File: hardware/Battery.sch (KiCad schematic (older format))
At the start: 14 parts, among them Q401 DMP2110UW-7, U401 LM66100, U402 MCP73831-2-OT, U403 TLV810E

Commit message: added order references to parts
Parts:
- R401, R402, R403: Manufacturer (none) -> TE Connectivity / Holsworthy; Order (none) -> https://www.mouser.at/ProductDetail/TE-Connectivity-Holswor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
- U403: Manufacturer (none) -> Texas Instruments; Order (none) -> https://www.mouser.at/ProductDetail/Texas-Instruments/TLV81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
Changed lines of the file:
@@
 F 2 "Resistor_SMD:R_0603_1608Metric" H 3250 2150 50  0001 C CNN
 F 3 "~" H 3250 2150 50  0001 C CNN
-F 4 "" H 3250 2150 50  0001 C CNN "Order"
+F 4 "https://www.mouser.at/ProductDetail/TE-Connectivity-Holsworthy/CRGP0603F3K9?qs=%2Fha2pyFaduj8qGn91HGzk%2F8kvmOrHSLEzveCoZJh19NXlgDLdxx7mg%3D%3D" H 3250 2150 50  0001 C CNN "Order"
+F 5 "TE Connectivity / Holsworthy" H 3250 2150 50  0001 C CNN "Manufacturer"
 	1    3250 2150
 	1    0    0    -1
@@
 F 2 "Package_TO_SOT_SMD:SOT-23" H 6150 2950 50  0001 C CNN
 F 3 "" H 6150 2950 50  0001 C CNN
+F 4 "Texas Instruments" H 5750 2250 50  0001 C CNN "Manufacturer"
+F 5 "https://www.mouser.at/ProductDetail/Texas-Instruments/TLV810EA29DBZR?qs=OlC7AqGiEDn%2F4%252BrWzJaHww%3D%3D" H 5750 2250 50  0001 C CNN "Order"
 	1    5750 2250
 	1    0    0    -1
@@
 F 2 "Resistor_SMD:R_0603_1608Metric" H 2650 2600 50  0001 C CNN
 F 3 "~" H 2650 2600 50  0001 C CNN
-F 4 "" H 2650 2600 50  0001 C CNN "Order"
+F 4 "https://www.mouser.at/ProductDetail/TE-Connectivity-Holsworthy/CRGP0603F2K7?qs=wUXugUrL1qwUN23XEDlhqg%3D%3D" H 2650 2600 50  0001 C CNN "Order"
+F 5 "TE Connectivity / Holsworthy" H 2650 2600 50  0001 C CNN "Manufacturer"
 	1    2650 2600
 	1    0    0    -1
@@
 F 2 "Resistor_SMD:R_0603_1608Metric" H 2650 3400 50  0001 C CNN
 F 3 "~" H 2650 3400 50  0001 C CNN
-F 4 "" H 2650 3400 50  0001 C CNN "Order"
+F 4 "https://www.mouser.at/ProductDetail/TE-Connectivity-Holsworthy/CRGP0603F2K7?qs=wUXugUrL1qwUN23XEDlhqg%3D%3D" H 2650 3400 50  0001 C CNN "Order"
+F 5 "TE Connectivity / Holsworthy" H 2650 3400 50  0001 C CNN "Manufacturer"
 	1    2650 3400
 	1    0    0    -1

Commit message: modified bom
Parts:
- BT401: value Battery_Cell -> LIPO
- C401, C402: MNR (none) -> CL10B106MQ8NRNC
- D401: MNR (none) -> AA1608SURSK
- D402: MNR (none) -> AA1608CGSK
- Q401: MNR (none) -> DMP2110UW-7
- R401, R402: MNR (none) -> CRGP0603F2K7
- R403: MNR (none) -> CRGP0603F3K9
- R404, R405: MNR (none) -> CRGP0603F47K
- U401: MNR (none) -> LM66100DCKR
- U402: MNR (none) -> MCP73831T-2ACI/OT
- U403: MNR (none) -> TLV810EA29DBZR
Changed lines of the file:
@@
 F 4 "https://www.mouser.at/ProductDetail/187-CL10B106MQ8NRNC" H 2950 1850 50  0001 C CNN "Order"
 F 5 "Samsung Electro-Mechanics" H 2950 1850 50  0001 C CNN "Manufacturer"
+F 6 "CL10B106MQ8NRNC" H 2950 1850 50  0001 C CNN "MNR"
 	1    2950 1850
 	1    0    0    -1
@@
 F 4 "https://www.mouser.at/ProductDetail/187-CL10B106MQ8NRNC" H 4400 1950 50  0001 C CNN "Order"
 F 5 "Samsung Electro-Mechanics" H 4400 1950 50  0001 C CNN "Manufacturer"
+F 6 "CL10B106MQ8NRNC" H 4400 1950 50  0001 C CNN "MNR"
 	1    4400 1950
 	1    0    0    -1
@@
 F 4 "https://www.mouser.at/ProductDetail/579-MCP73831T-2ACIOT" H 3750 1900 50  0001 C CNN "Order"
 F 5 "Microchip Technology" H 3750 1900 50  0001 C CNN "Manufacturer"
+F 6 "MCP73831T-2ACI/OT" H 3750 1900 50  0001 C CNN "MNR"
 	1    3750 1900
 	1    0    0    -1
@@
 F 4 "https://www.mouser.at/ProductDetail/TE-Connectivity-Holsworthy/CRGP0603F3K9?qs=%2Fha2pyFaduj8qGn91HGzk%2F8kvmOrHSLEzveCoZJh19NXlgDLdxx7mg%3D%3D" H 3250 2150 50  0001 C CNN "Order"
 F 5 "TE Connectivity / Holsworthy" H 3250 2150 50  0001 C CNN "Manufacturer"
+F 6 "CRGP0603F3K9" H 3250 2150 50  0001 C CNN "MNR"
 	1    3250 2150
 	1    0    0    -1
@@
 AR Path="/6063DAC2/60645BC2" Ref="BT401"  Part="1"
 F 0 "BT401" H 4868 2146 50  0000 L CNN
-F 1 "Battery_Cell" H 4868 2055 50  0000 L CNN
+F 1 "LIPO" H 4868 2055 50  0000 L CNN
 F 2 "Connector_PinHeader_2.54mm:PinHeader_1x02_P2.54mm_Vertical" V 4750 2110 50  0001 C CNN
 F 3 "~" V 4750 2110 50  0001 C CNN
@@
 F 4 "Diodes Incorporated" H 6200 1900 50  0001 C CNN "Manufacturer"
 F 5 "https://www.mouser.at/ProductDetail/Diodes-Incorporated/DMP2110UW-7?qs=bZr6mbWTK5lZsAURvLPe3w%3D%3D" H 6200 1900 50  0001 C CNN "Order"
+F 6 "DMP2110UW-7" H 6200 1900 50  0001 C CNN "MNR"
 	1    6200 1900
 	0    1    -1   0
@@
 F 4 "Texas Instruments" H 5750 2250 50  0001 C CNN "Manufacturer"
 F 5 "https://www.mouser.at/ProductDetail/Texas-Instruments/TLV810EA29DBZR?qs=OlC7AqGiEDn%2F4%252BrWzJaHww%3D%3D" H 5750 2250 50  0001 C CNN "Order"
+F 6 "TLV810EA29DBZR" H 5750 2250 50  0001 C CNN "MNR"
 	1    5750 2250
 	1    0    0    -1
@@
 F 4 "https://www.mouser.at/ProductDetail/279-CRGP0603F47K" H 6800 2300 50  0001 C CNN "Order"
 F 5 "TE Connectivity / Holsworthy" H 6800 2300 50  0001 C CNN "Manufacturer"
+F 6 "CRGP0603F47K" H 6800 2300 50  0001 C CNN "MNR"
 	1    6800 2300
 	1    0    0    -1
@@
 F 4 "https://www.mouser.at/ProductDetail/279-CRGP0603F47K" H 6800 2000 50  0001 C CNN "Order"
 F 5 "TE Connectivity / Holsworthy" H 6800 2000 50  0001 C CNN "Manufacturer"
+F 6 "CRGP0603F47K" H 6800 2000 50  0001 C CNN "MNR"
 	1    6800 2000
 	1    0    0    -1
@@
 F 4 "Texas Instruments" H 1950 1600 50  0001 C CNN "Manufacturer"
 F 5 "https://www.mouser.at/ProductDetail/595-LM66100DCKR" H 1950 1600 50  0001 C CNN "Order"
+F 6 "LM66100DCKR" H 1950 1600 50  0001 C CNN "MNR"
 	1    1950 1600
 	1    0    0    -1
@@
 F 5 "Kingbright" V 2650 2850 50  0001 C CNN "Manufacturer"
 F 6 "https://www.mouser.at/ProductDetail/Kingbright/AA1608SURSK?qs=eP2BKZSCXI6pqonvuMmTFg%3D%3D" H 2650 2850 50  0001 C CNN "Order"
+F 7 "AA1608SURSK" H 2650 2850 50  0001 C CNN "MNR"
 	1    2650 2850
 	0    -1   -1   0
@@
 F 4 "https://www.mouser.at/ProductDetail/TE-Connectivity-Holsworthy/CRGP0603F2K7?qs=wUXugUrL1qwUN23XEDlhqg%3D%3D" H 2650 2600 50  0001 C CNN "Order"
 F 5 "TE Connectivity / Holsworthy" H 2650 2600 50  0001 C CNN "Manufacturer"
+F 6 "CRGP0603F2K7" H 2650 2600 50  0001 C CNN "MNR"
 	1    2650 2600
 	1    0    0    -1
@@
 F 4 "https://www.mouser.at/ProductDetail/TE-Connectivity-Holsworthy/CRGP0603F2K7?qs=wUXugUrL1qwUN23XEDlhqg%3D%3D" H 2650 3400 50  0001 C CNN "Order"
 F 5 "TE Connectivity / Holsworthy" H 2650 3400 50  0001 C CNN "Manufacturer"
+F 6 "CRGP0603F2K7" H 2650 3400 50  0001 C CNN "MNR"
 	1    2650 3400
 	1    0    0    -1
@@
 F 5 "AA1608CGSK" H 2650 3150 50  0001 C CNN "Part Number"
 F 6 "https://www.mouser.at/ProductDetail/Kingbright/AA1608CGSK?qs=%2Fha2pyFadujroVvVMWEuOp8b2ZvB17TZCtvrJxnHY68n8r1EECXbcw%3D%3D" H 2650 3150 50  0001 C CNN "Order"
+F 7 "AA1608CGSK" H 2650 3150 50  0001 C CNN "MNR"
 	1    2650 3150
 	0    -1   -1   0

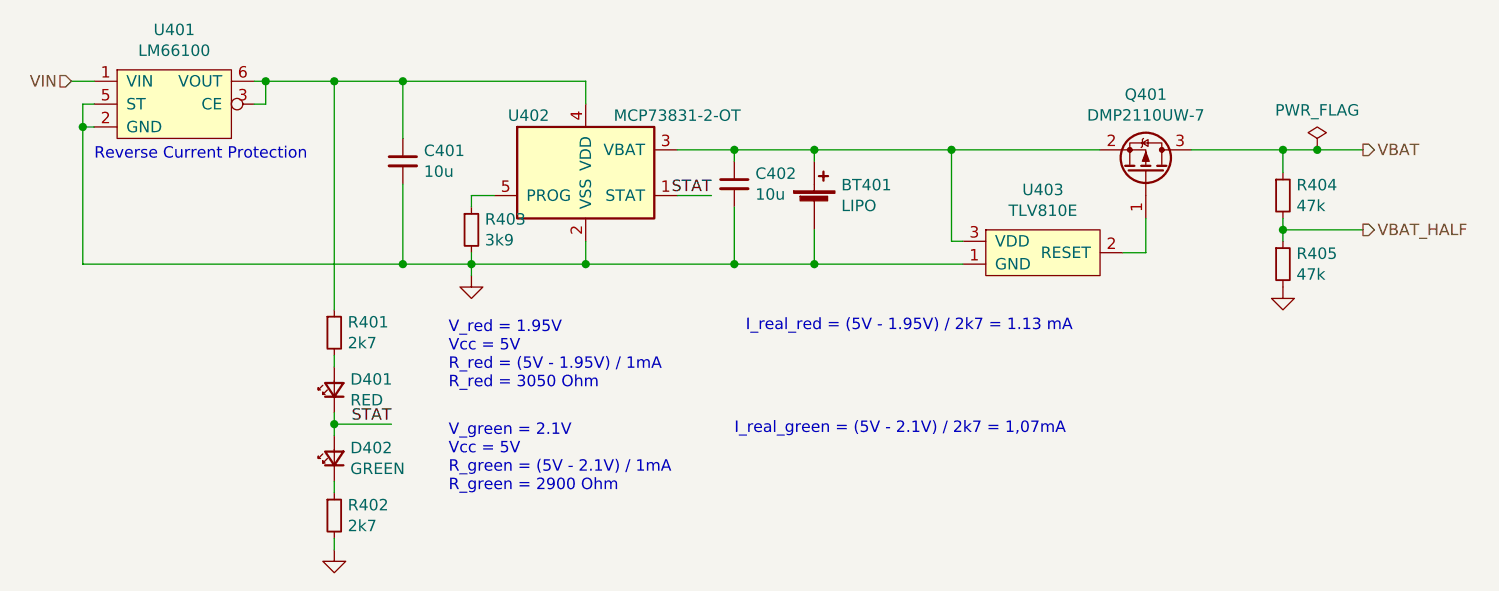
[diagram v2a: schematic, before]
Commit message: New uC, ditched FTDI chip, and more!
Need to improve the schematic a little bit more.
For example, I want to be able to turn the LED Drivers off using
a MOSFET.

For the PCB Layout: I want to move as many components as possible
to the top layer, so that they are visible when in the case.
Also, I have to consider solderability of the components, the more
complex should all be on one layer for easier soldering.

Next up: Finishing the schematic, improving component placement,
and routing!
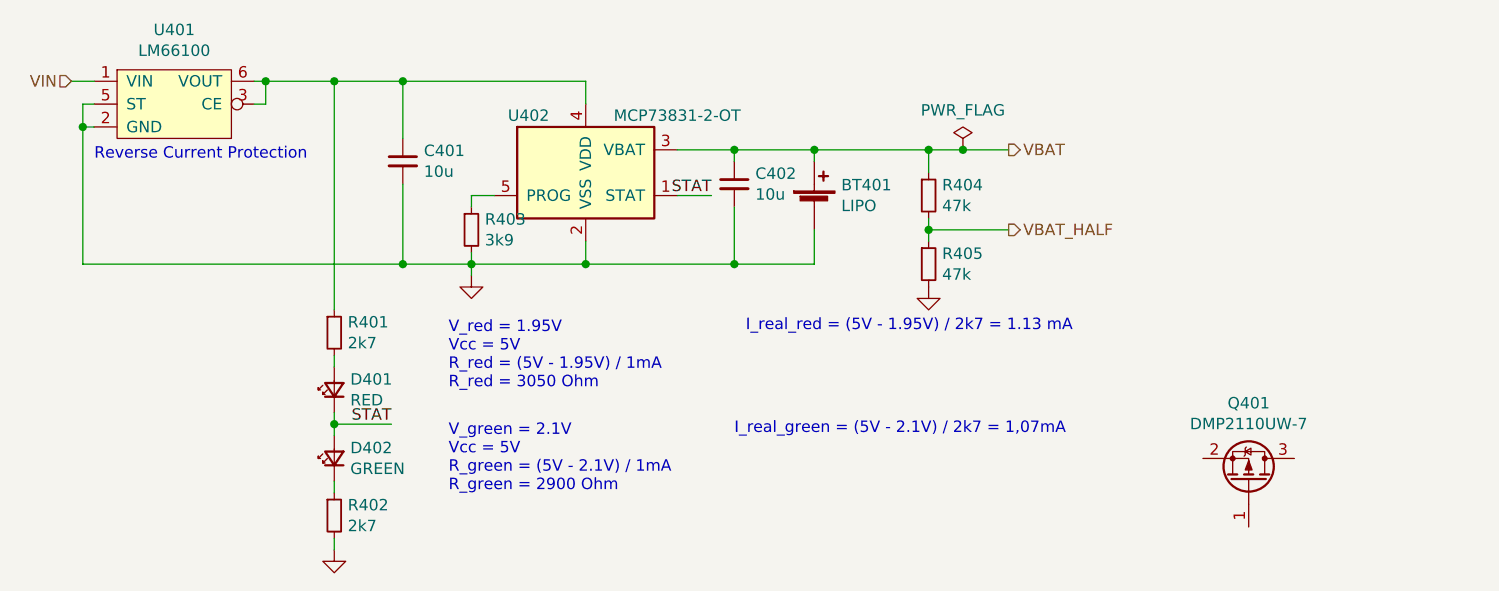
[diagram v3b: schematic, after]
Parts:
- removed U403: TLV810E, Package_TO_SOT_SMD:SOT-23, symbol watch:TLV810E
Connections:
- net VBAT: now also BT401.1 (+), C402.1, U402.3 (VBAT); no longer Q401.3 (D)
- now unconnected: Q401.2 (S)
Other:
- moved on the sheet: Q401, R404, R405
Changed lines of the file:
@@
 $Descr A4 11693 8268
 encoding utf-8
-Sheet 4 7
+Sheet 4 6
 Title "aWristWatch"
 Date "2021-04-05"
@@
 Text HLabel 1500 1500 0    50   Input ~ 0
 VIN
-Text HLabel 7150 1800 2    50   Output ~ 0
+Text HLabel 5600 1800 2    50   Output ~ 0
 VBAT
 Wire Wire Line
@@
 L Device:Q_PMOS_GSD Q401
 U 1 1 60686379
-P 6200 1900
-F 0 "Q401" V 6542 1900 50  0000 C CNN
-F 1 "DMP2110UW-7" V 6451 1900 50  0000 C CNN
-F 2 "Package_TO_SOT_SMD:SOT-323_SC-70" H 6400 2000 50  0001 C CNN
-F 3 "https://www.diodes.com/assets/Datasheets/DMP2110UW.pdf" H 6200 1900 50  0001 C CNN
-F 4 "Diodes Incorporated" H 6200 1900 50  0001 C CNN "Manufacturer"
-F 5 "https://www.mouser.at/ProductDetail/Diodes-Incorporated/DMP2110UW-7?qs=bZr6mbWTK5lZsAURvLPe3w%3D%3D" H 6200 1900 50  0001 C CNN "Order"
-F 6 "DMP2110UW-7" H 6200 1900 50  0001 C CNN "MNR"
-	1    6200 1900
+P 6650 3250
+F 0 "Q401" V 6992 3250 50  0000 C CNN
+F 1 "DMP2110UW-7" V 6901 3250 50  0000 C CNN
+F 2 "Package_TO_SOT_SMD:SOT-323_SC-70" H 6850 3350 50  0001 C CNN
+F 3 "https://www.diodes.com/assets/Datasheets/DMP2110UW.pdf" H 6650 3250 50  0001 C CNN
+F 4 "Diodes Incorporated" H 6650 3250 50  0001 C CNN "Manufacturer"
+F 5 "https://www.mouser.at/ProductDetail/Diodes-Incorporated/DMP2110UW-7?qs=bZr6mbWTK5lZsAURvLPe3w%3D%3D" H 6650 3250 50  0001 C CNN "Order"
+F 6 "DMP2110UW-7" H 6650 3250 50  0001 C CNN "MNR"
+	1    6650 3250
 	0    1    -1   0
 $EndComp
-Connection ~ 4750 1800
-$Comp
-L watch:TLV810E U403
-U 1 1 6068D817
-P 5750 2250
-F 0 "U403" H 5750 2525 50  0000 C CNN
-F 1 "TLV810E" H 5750 2434 50  0000 C CNN
-F 2 "Package_TO_SOT_SMD:SOT-23" H 6150 2950 50  0001 C CNN
-F 3 "" H 6150 2950 50  0001 C CNN
-F 4 "Texas Instruments" H 5750 2250 50  0001 C CNN "Manufacturer"
-F 5 "https://www.mouser.at/ProductDetail/Texas-Instruments/TLV810EA29DBZR?qs=OlC7AqGiEDn%2F4%252BrWzJaHww%3D%3D" H 5750 2250 50  0001 C CNN "Order"
-F 6 "TLV810EA29DBZR" H 5750 2250 50  0001 C CNN "MNR"
-	1    5750 2250
-	1    0    0    -1
-$EndComp
-Wire Wire Line
-	4750 1800 5350 1800
-Wire Wire Line
-	5400 2200 5350 2200
-Wire Wire Line
-	5350 2200 5350 1800
-Wire Wire Line
-	5400 2300 4750 2300
-Connection ~ 4750 2300
-Wire Wire Line
-	6100 2250 6200 2250
-Wire Wire Line
-	6200 2250 6200 2100
-Wire Wire Line
-	6000 1800 5350 1800
-Connection ~ 5350 1800
 $Comp
 L power:GND #PWR?
 U 1 1 606C5053
-P 6800 2400
+P 5250 2400
 AR Path="/606C5053" Ref="#PWR?"  Part="1"
 AR Path="/6063DAC2/606C5053" Ref="#PWR0124"  Part="1"
-F 0 "#PWR0124" H 6800 2150 50  0001 C CNN
-F 1 "GND" H 6805 2227 50  0001 C CNN
-F 2 "" H 6800 2400 50  0001 C CNN
-F 3 "" H 6800 2400 50  0001 C CNN
-	1    6800 2400
-	1    0    0    -1
-$EndComp
-Wire Wire Line
-	6800 2150 6800 2200
-Connection ~ 6800 2150
-Wire Wire Line
-	6800 2100 6800 2150
+F 0 "#PWR0124" H 5250 2150 50  0001 C CNN
+F 1 "GND" H 5255 2227 50  0001 C CNN
+F 2 "" H 5250 2400 50  0001 C CNN
+F 3 "" H 5250 2400 50  0001 C CNN
+	1    5250 2400
+	1    0    0    -1
+$EndComp
+Wire Wire Line
+	5250 2150 5250 2200
+Connection ~ 5250 2150
+Wire Wire Line
+	5250 2100 5250 2150
 $Comp
 L Device:R_Small R?
 U 1 1 606C505F
-P 6800 2300
+P 5250 2300
 AR Path="/606C505F" Ref="R?"  Part="1"
 AR Path="/6063DAC2/606C505F" Ref="R405"  Part="1"
-F 0 "R405" H 6859 2346 50  0000 L CNN
-F 1 "47k" H 6859 2255 50  0000 L CNN
-F 2 "Resistor_SMD:R_0603_1608Metric" H 6800 2300 50  0001 C CNN
-F 3 "https://www.mouser.at/datasheet/2/418/5/NG_DS_9-1773463-9_A-1358566.pdf" H 6800 2300 50  0001 C CNN
-F 4 "https://www.mouser.at/ProductDetail/279-CRGP0603F47K" H 6800 2300 50  0001 C CNN "Order"
-F 5 "TE Connectivity / Holsworthy" H 6800 2300 50  0001 C CNN "Manufacturer"
-F 6 "CRGP0603F47K" H 6800 2300 50  0001 C CNN "MNR"
-	1    6800 2300
+F 0 "R405" H 5309 2346 50  0000 L CNN
+F 1 "47k" H 5309 2255 50  0000 L CNN
+F 2 "Resistor_SMD:R_0603_1608Metric" H 5250 2300 50  0001 C CNN
+F 3 "https://www.mouser.at/datasheet/2/418/5/NG_DS_9-1773463-9_A-1358566.pdf" H 5250 2300 50  0001 C CNN
+F 4 "https://www.mouser.at/ProductDetail/279-CRGP0603F47K" H 5250 2300 50  0001 C CNN "Order"
+F 5 "TE Connectivity / Holsworthy" H 5250 2300 50  0001 C CNN "Manufacturer"
+F 6 "CRGP0603F47K" H 5250 2300 50  0001 C CNN "MNR"
+	1    5250 2300
 	1    0    0    -1
 $EndComp
@@
 L Device:R_Small R?
 U 1 1 606C5066
-P 6800 2000
+P 5250 2000
 AR Path="/606C5066" Ref="R?"  Part="1"
 AR Path="/6063DAC2/606C5066" Ref="R404"  Part="1"
-F 0 "R404" H 6859 2046 50  0000 L CNN
-F 1 "47k" H 6859 1955 50  0000 L CNN
-F 2 "Resistor_SMD:R_0603_1608Metric" H 6800 2000 50  0001 C CNN
-F 3 "https://www.mouser.at/datasheet/2/418/5/NG_DS_9-1773463-9_A-1358566.pdf" H 6800 2000 50  0001 C CNN
-F 4 "https://www.mouser.at/ProductDetail/279-CRGP0603F47K" H 6800 2000 50  0001 C CNN "Order"
-F 5 "TE Connectivity / Holsworthy" H 6800 2000 50  0001 C CNN "Manufacturer"
-F 6 "CRGP0603F47K" H 6800 2000 50  0001 C CNN "MNR"
-	1    6800 2000
-	1    0    0    -1
-$EndComp
-Wire Wire Line
-	6400 1800 6800 1800
-Wire Wire Line
-	6800 1800 6800 1900
-Wire Wire Line
-	6800 1800 6950 1800
-Connection ~ 6800 1800
-Text HLabel 7150 2150 2    50   Output ~ 0
+F 0 "R404" H 5309 2046 50  0000 L CNN
+F 1 "47k" H 5309 1955 50  0000 L CNN
+F 2 "Resistor_SMD:R_0603_1608Metric" H 5250 2000 50  0001 C CNN
+F 3 "https://www.mouser.at/datasheet/2/418/5/NG_DS_9-1773463-9_A-1358566.pdf" H 5250 2000 50  0001 C CNN
+F 4 "https://www.mouser.at/ProductDetail/279-CRGP0603F47K" H 5250 2000 50  0001 C CNN "Order"
+F 5 "TE Connectivity / Holsworthy" H 5250 2000 50  0001 C CNN "Manufacturer"
+F 6 "CRGP0603F47K" H 5250 2000 50  0001 C CNN "MNR"
+	1    5250 2000
+	1    0    0    -1
+$EndComp
+Wire Wire Line
+	5250 1800 5250 1900
+Wire Wire Line
+	5250 1800 5400 1800
+Connection ~ 5250 1800
+Text HLabel 5600 2150 2    50   Output ~ 0
 VBAT_HALF
 Wire Wire Line
-	6800 2150 7150 2150
+	5250 2150 5600 2150
 Wire Wire Line
 	1600 1700 1550 1700
@@
 L power:PWR_FLAG #FLG0105
 U 1 1 606AB429
-P 6950 1800
-F 0 "#FLG0105" H 6950 1875 50  0001 C CNN
-F 1 "PWR_FLAG" H 6950 1973 50  0000 C CNN
-F 2 "" H 6950 1800 50  0001 C CNN
-F 3 "~" H 6950 1800 50  0001 C CNN
-	1    6950 1800
-	1    0    0    -1
-$EndComp
-Connection ~ 6950 1800
-Wire Wire Line
-	6950 1800 7150 1800
+P 5400 1800
+F 0 "#FLG0105" H 5400 1875 50  0001 C CNN
+F 1 "PWR_FLAG" H 5400 1973 50  0000 C CNN
+F 2 "" H 5400 1800 50  0001 C CNN
+F 3 "~" H 5400 1800 50  0001 C CNN
+	1    5400 1800
+	1    0    0    -1
+$EndComp
+Connection ~ 5400 1800
+Wire Wire Line
+	5400 1800 5600 1800
+Wire Wire Line
+	4750 1800 5250 1800
+Connection ~ 4750 1800
 $EndSCHEMATC

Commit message: Updated to KiCad v6.0
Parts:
- removed Q401: DMP2110UW-7, Package_TO_SOT_SMD:SOT-323_SC-70, symbol Device:Q_PMOS_GSD
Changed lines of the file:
@@
 	2950 2300 3250 2300
-$Comp
-L Device:Q_PMOS_GSD Q401
-U 1 1 60686379
-P 6650 3250
-F 0 "Q401" V 6992 3250 50  0000 C CNN
-F 1 "DMP2110UW-7" V 6901 3250 50  0000 C CNN
-F 2 "Package_TO_SOT_SMD:SOT-323_SC-70" H 6850 3350 50  0001 C CNN
-F 3 "https://www.diodes.com/assets/Datasheets/DMP2110UW.pdf" H 6650 3250 50  0001 C CNN
-F 4 "Diodes Incorporated" H 6650 3250 50  0001 C CNN "Manufacturer"
-F 5 "https://www.mouser.at/ProductDetail/Diodes-Incorporated/DMP2110UW-7?qs=bZr6mbWTK5lZsAURvLPe3w%3D%3D" H 6650 3250 50  0001 C CNN "Order"
-F 6 "DMP2110UW-7" H 6650 3250 50  0001 C CNN "MNR"
-	1    6650 3250
-	0    1    -1   0
-$EndComp
 $Comp
 L power:GND #PWR?
